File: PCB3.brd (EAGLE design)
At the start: 94.7 x 52.2 mm, 134 parts

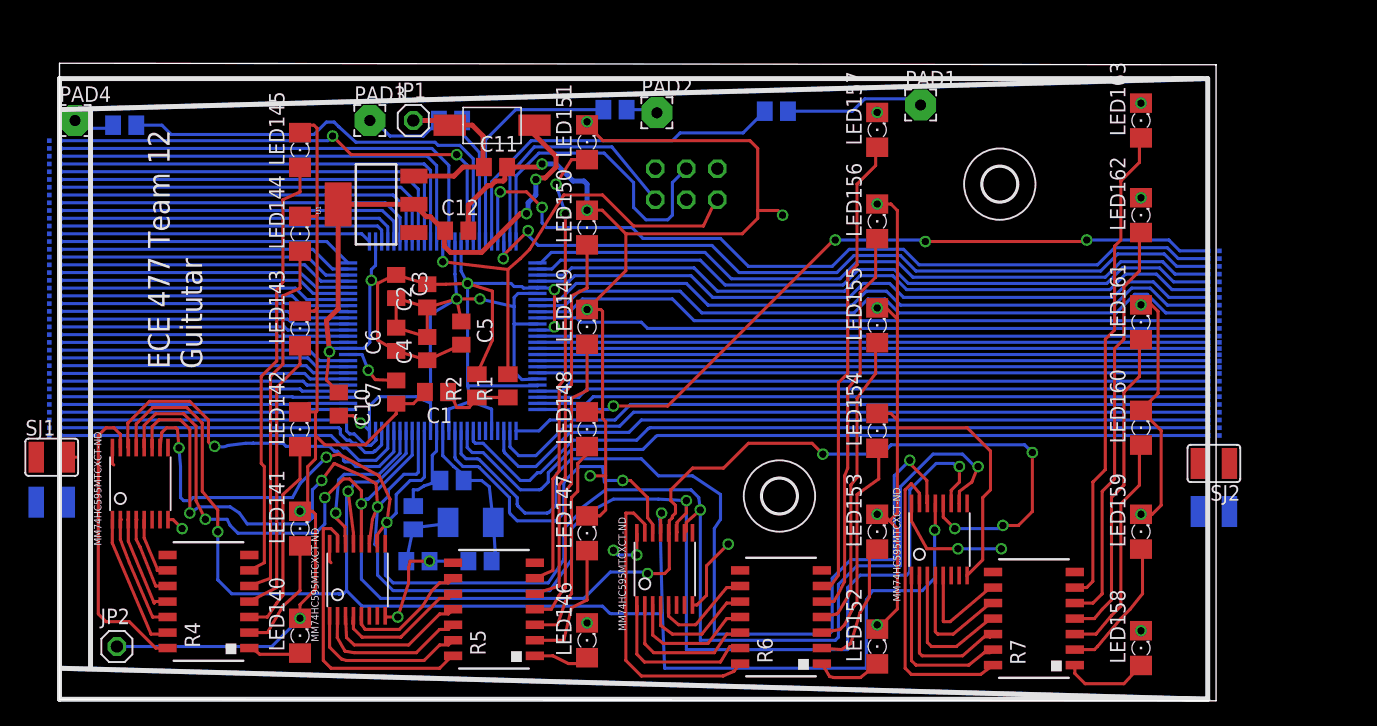
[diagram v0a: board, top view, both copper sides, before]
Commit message: Finished changing dimensions for PCB3 and switched out resistors for smaller ones.
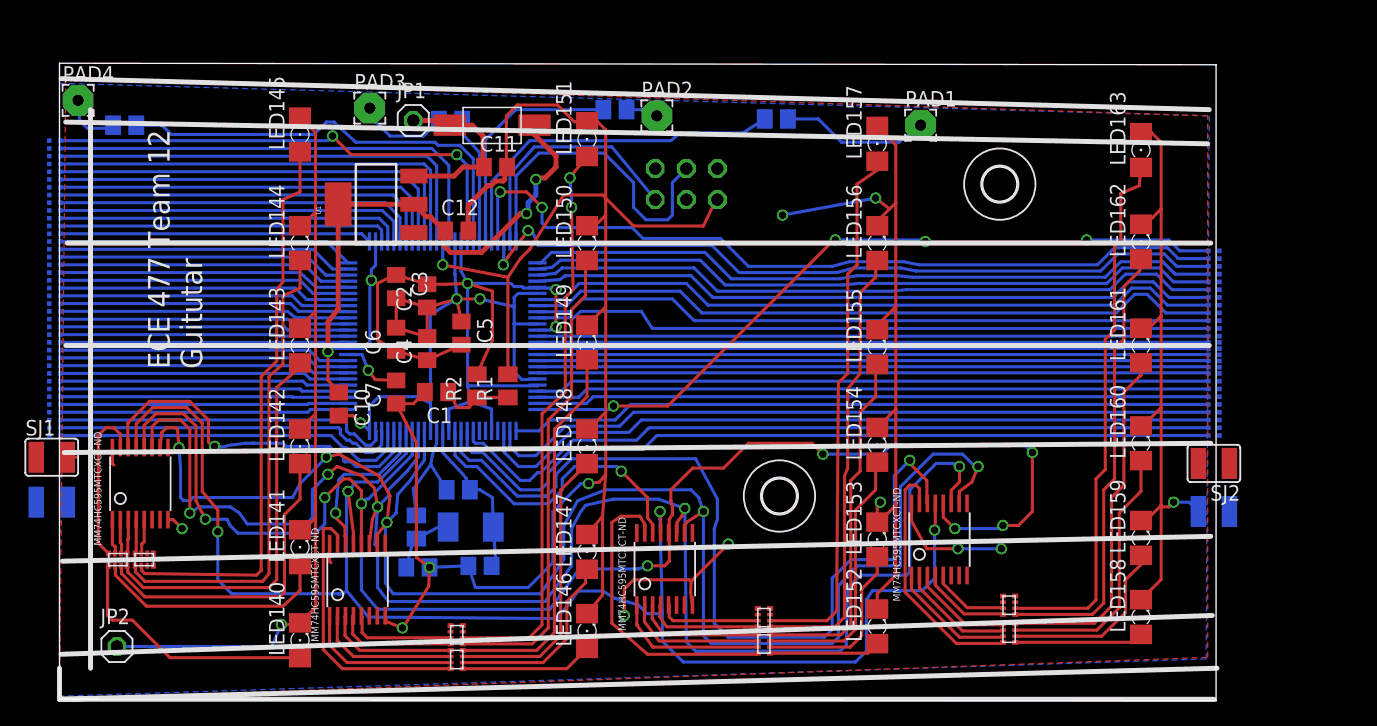
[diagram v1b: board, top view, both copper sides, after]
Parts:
- removed R4, R5, R6, R7: (no value), resistor-bourns:4814P
- added U$71, U$72, U$73, U$74, U$75, U$76, U$77, U$78: MNR04MRAPJ680, ECE477_Guitutar:MNR04
- moved LED158 2.54 mm to (88.5, 6.73)
- moved LED163 2.41 mm to (88.5, 45.0)
- moved LED162 2.16 mm to (88.5, 37.5)
- moved LED161 1.91 mm to (88.5, 29.0)
- moved LED155 1.78 mm to (66.9, 28.8)
- moved LED156 1.78 mm to (66.9, 37.3)
- moved PAD4 1.67 mm to (1.52, 49.0)
- moved LED152 1.65 mm to (66.9, 5.97)
- moved PAD1 1.65 mm to (70.5, 47.0)
- moved LED141 1.52 mm to (19.7, 12.4)
- moved LED147 1.52 mm to (43.2, 12.1)
- moved LED143 1.40 mm to (19.7, 29.0)
- moved LED142 1.40 mm to (19.7, 20.7)
- moved LED148 1.40 mm to (43.2, 20.7)
- moved LED145 1.27 mm to (19.7, 46.2)
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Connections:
- removed net N$102: LED153.A, R6.2
- removed net N$113: R7.13, U$26.1
- removed net N$114: R7.12, U$26.2
- removed net N$115: R7.11, U$26.3
- removed net N$116: R7.10, U$26.4
- removed net N$123: R7.9, U$26.5
- removed net N$127: LED160.A, R7.3
- removed net N$75: R5.9, U$28.5
- removed net N$78: LED146.A, R5.1
- removed net N$80: LED148.A, R5.3
- removed net N$81: LED149.A, R5.4
- removed net N$82: LED150.A, R5.5
- removed net N$83: LED151.A, R5.6
- removed net N$84: LED147.A, R5.2
- removed net N$90: R6.13, U$29.1
- removed net N$91: R6.12, U$29.2
- removed net N$92: R6.11, U$29.3
- removed net N$93: R6.10, U$29.4
- removed net N$94: R6.9, U$29.5
- removed net N$98: LED154.A, R6.3
- removed net N$99: LED155.A, R6.4
- new net N$10: LED148.A, U$75.P$3
- new net N$15: LED149.A, U$75.P$4
- new net N$17: LED150.A, U$76.P$1
- new net N$18: LED151.A, U$76.P$2
- new net N$19: U$27.1, U$73.P$6
- new net N$26: U$26.1, U$71.P$6
- new net N$27: U$26.2, U$71.P$7
- new net N$28: U$26.3, U$71.P$8
- new net N$29: U$26.4, U$72.P$5
- new net N$30: U$26.5, U$72.P$6
- new net N$36: U$29.1, U$77.P$6
- new net N$39: U$29.2, U$77.P$7
- new net N$40: U$29.3, U$77.P$8
- new net N$41: U$29.4, U$78.P$5
- new net N$42: U$29.5, U$78.P$6
- new net N$43: LED153.A, U$77.P$2
- new net N$44: LED154.A, U$77.P$3
- new net N$45: LED155.A, U$77.P$4
- new net N$6: U$28.5, U$76.P$6
- new net N$8: LED146.A, U$75.P$1
- new net N$9: LED147.A, U$75.P$2
- net N$100: now also U$78.P$1; no longer R6.5
- net N$101: now also U$78.P$2; no longer R6.6
- net N$125: now also U$71.P$5; no longer R7.14
- net N$126: now also U$71.P$1; no longer R7.1
- net N$134: now also U$71.P$4; no longer R7.4
- net N$135: now also U$72.P$1; no longer R7.5
- net N$136: now also U$72.P$2; no longer R7.6
- net N$137: now also U$71.P$2; no longer R7.2
- net N$20: now also U$27.2, U$73.P$7; no longer R4.13, U$27.1
- net N$21: now also U$27.3, U$73.P$8; no longer R4.12, U$27.2
- net N$22: now also U$27.4, U$74.P$5; no longer R4.11, U$27.3
- net N$23: now also U$27.5, U$74.P$6; no longer R4.10, U$27.4
- net N$24: now also LED142.A, U$73.P$3; no longer R4.9, U$27.5
- net N$31: now also U$73.P$5; no longer R4.14
- net N$32: now also U$73.P$1; no longer R4.1
- net N$33: now also U$73.P$2; no longer R4.2
- net N$34: now also LED160.A, U$71.P$3; no longer LED142.A, R4.3
- net N$35: now also U$73.P$4; no longer R4.4
- net N$46: now also U$74.P$1; no longer R4.5
- net N$47: now also U$74.P$2; no longer R4.6
- net N$62: now also U$75.P$6; no longer R5.13
- net N$63: now also U$75.P$7; no longer R5.12
- net N$64: now also U$75.P$8; no longer R5.11
- net N$74: now also U$76.P$5; no longer R5.10
- net N$77: now also U$75.P$5; no longer R5.14
- net N$96: now also U$77.P$5; no longer R6.14
- net N$97: now also U$77.P$1; no longer R6.1
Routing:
- net N$11: track 94.0 -> 0.00 mm
- net N$6: track 94.0 -> 8.82 mm
- net GND: track 261.6 -> 310.3 mm, vias 23 -> 11
- net N$18: track 0.00 -> 46.8 mm, vias 0 -> 2
- net N$17: track 0.00 -> 38.9 mm
- net N$83: track 37.4 -> 0.00 mm, vias 2 -> 0
- net N$15: track 0.00 -> 31.5 mm
- net N$82: track 31.1 -> 0.00 mm
- net N$45: track 0.00 -> 29.2 mm
- net N$99: track 24.5 -> 0.00 mm
- net N$81: track 24.4 -> 0.00 mm
- net N$10: track 0.00 -> 23.7 mm
- net LED_SER7: track 29.6 -> 51.8 mm
- net N$44: track 0.00 -> 21.8 mm
- net N$24: track 5.22 -> 26.0 mm
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
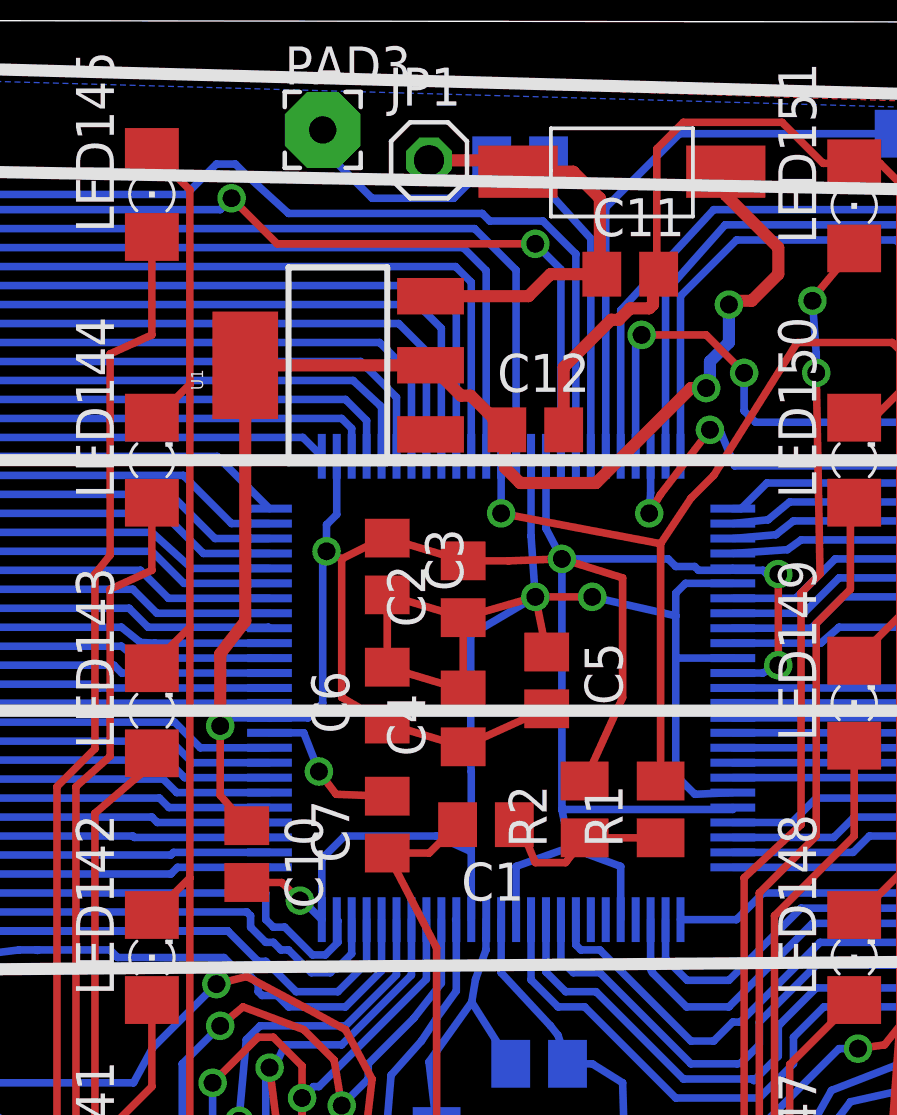
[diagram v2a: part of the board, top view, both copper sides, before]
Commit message: Updated ref des to match those in BOM
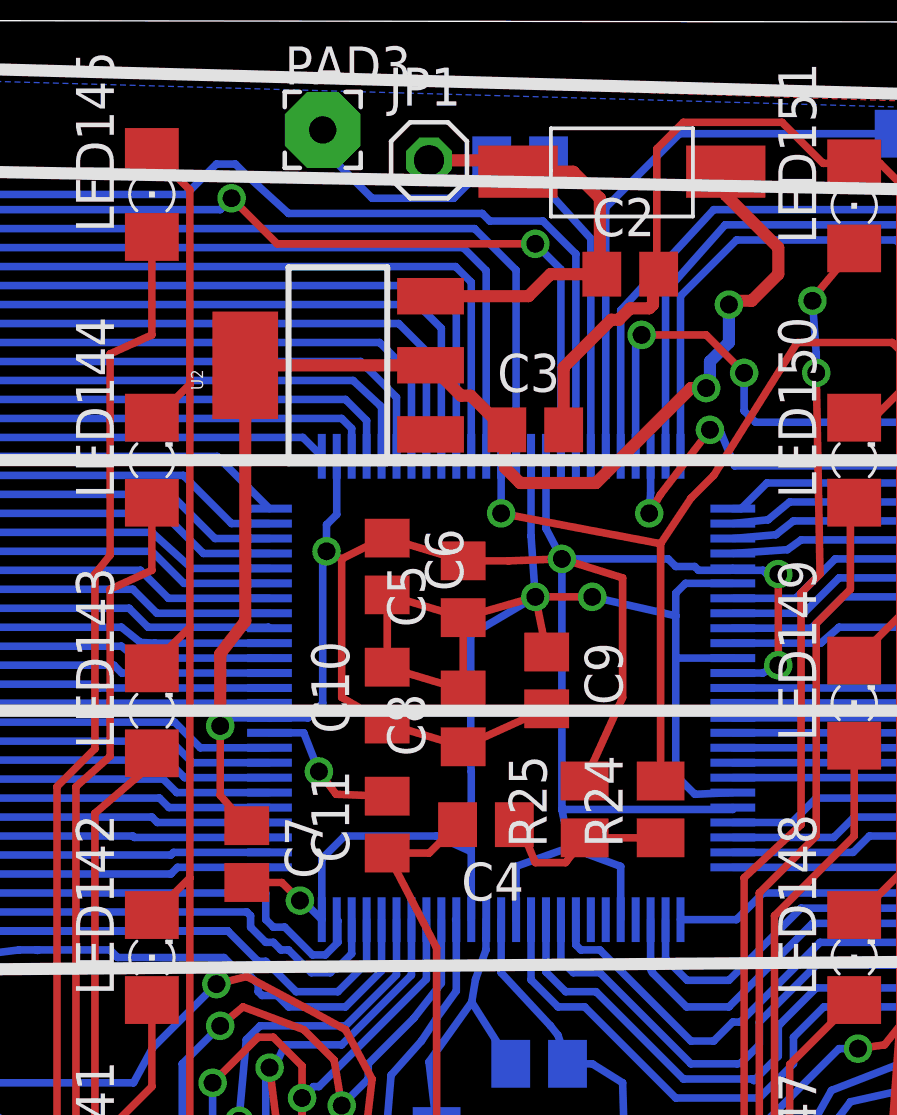
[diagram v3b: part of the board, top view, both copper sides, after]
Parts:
- removed C1: (no value), rcl:C0805
- removed R11: 330k, rcl:M0805
- removed U$2: PIC32MX570F512L, ECE477_Guitutar:TQFP100-14X14
- added C13: 9pF, rcl:C0805
- added R26: 1M, rcl:M0805
- added U2: (no value), SparkFun-IC-Power:SOT223
- C12: value 100uF -> 9pF
- C2: value (none) -> 10uF
- C3: value (none) -> 100uF
- C4: value (none) -> 0.1u
- R24: value (none) -> 1k
- R25: value (none) -> 10k
- R27: value (none) -> 100
- R8: value (none) -> 330k
- U1: value (none) -> PIC32MX570F512L; device SparkFun-IC-Power:SOT223 -> ECE477_Guitutar:TQFP100-14X14
- Y1: value (none) -> 16MHz
- moved R8 33.7 mm to (45.5, 48.3)
- moved C12 27.5 mm to (34.4, 10.9), flipped to the bottom, turned to 180 degrees
- moved R10 26.7 mm to (5.33, 47.0)
- moved R9 26.7 mm to (32.0, 47.4)
- moved C11 20.1 mm to (27.6, 25.1), turned to 90 degrees
- moved C9 19.5 mm to (32.9, 30.0), flipped to the top, turned to 270 degrees
- moved C8 18.3 mm to (30.1, 28.7), flipped to the top, turned to 90 degrees
- moved U1 12.1 mm to (31.4, 29.7), flipped to the bottom, turned to 180 degrees
- moved C2 11.9 mm to (35.7, 43.6), turned to 0 degrees
- moved C10 7.09 mm to (27.6, 29.5), turned to 90 degrees
- moved C3 6.74 mm to (32.5, 38.4), turned to 0 degrees
- moved C7 4.80 mm to (22.9, 24.2), turned to 270 degrees
- moved C6 4.32 mm to (27.6, 33.8), turned to 270 degrees
- moved C5 4.13 mm to (30.1, 33.0), turned to 90 degrees
- moved C4 3.64 mm to (30.9, 25.1), turned to 180 degrees
- renumbered D1 to D140, R1 to R24, R12 to R7, R2 to R25, R3 to R27
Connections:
- removed net N$124: U$26.16
- removed net N$25: U$27.16
- removed net N$76: U$28.16
- removed net N$95: U$29.16
- net 5.2V_PB: now also C2.1, U2.3; no longer C11.1, U1.3
- net AMP: now also U1.50; no longer U$2.50
- net EAN: now also U1.79; no longer U$2.79
- net FRET1: now also U1.93; no longer U$2.93
- net FRET10: now also U1.22; no longer U$2.22
- net FRET11: now also U1.23; no longer U$2.23
- net FRET12: now also U1.26; no longer U$2.26
- net FRET13: now also U1.27; no longer U$2.27
- net FRET14: now also U1.28; no longer U$2.28
- net FRET15: now also U1.29; no longer U$2.29
- net FRET16: now also U1.32; no longer U$2.32
- net FRET17: now also U1.33; no longer U$2.33
- net FRET18: now also U1.34; no longer U$2.34
- net FRET19: now also U1.35; no longer U$2.35
- net FRET2: now also U1.92; no longer U$2.92
- net FRET20: now also U1.38; no longer U$2.38
- net FRET21: now also U1.39; no longer U$2.39
- net FRET22: now also U1.40; no longer U$2.40
- net FRET3: now also U1.91; no longer U$2.91
- net FRET4: now also U1.90; no longer U$2.90
- net FRET5: now also U1.17; no longer U$2.17
- net FRET6: now also R10.1, U1.18; no longer R9.1, U$2.18
- net FRET7: now also R9.1, U1.19; no longer R10.1, U$2.19
- net FRET8: now also R8.1, U1.20; no longer R11.1, U$2.20
- net FRET9: now also U1.21; no longer U$2.21
- net G: now also U1.69; no longer U$2.69
- net GND: now also C11.1, C12.1, C13.1, C2.2, C3.2, C4.2; no longer C1.2, C11.2, C12.2, C7.1, C8.1, C9.1
- net LED_SER1: now also U1.100; no longer U$2.100
- net LED_SER10: now also U1.70; no longer U$2.70
- net LED_SER11: now also U1.61; no longer U$2.61
- net LED_SER12: now also U1.51; no longer U$2.51
- net LED_SER13: now also U1.58; no longer U$2.58
- net LED_SER14: now also U1.59; no longer U$2.59
- net LED_SER15: now also U1.53; no longer U$2.53
- net LED_SER16: now also U1.52; no longer U$2.52
- net LED_SER17: now also U1.41; no longer U$2.41
- net LED_SER18: now also U1.42; no longer U$2.42
- net LED_SER19: now also U1.43; no longer U$2.43
- net LED_SER2: now also U1.99; no longer U$2.99
- net LED_SER20: now also U1.44; no longer U$2.44
- net LED_SER21: now also U1.47; no longer U$2.47
- net LED_SER22: now also U1.48; no longer U$2.48
- net LED_SER23: now also U1.49; no longer U$2.49
- net LED_SER3: now also U1.98; no longer U$2.98
- net LED_SER4: now also U1.97; no longer U$2.97
- net LED_SER5: now also U1.74; no longer U$2.74
- net LED_SER6: now also U1.73; no longer U$2.73
- net LED_SER7: now also U1.72; no longer U$2.72
- net LED_SER8: now also U1.60; no longer U$2.60
- net LED_SER9: now also U1.71; no longer U$2.71
- net N$1: now also C4.1; no longer C1.1
- net N$12: now also C11.2, U1.85; no longer C7.2, U$2.85
- net N$13: now also U1.13; no longer U$2.13
- net N$14: now also U1.25; no longer U$2.25
- net N$2: now also U1.24; no longer U$2.24
- net N$37: now also C13.2; no longer C9.2
- net N$38: now also C12.2, R26.2, U1.63; no longer C8.2, R8.2, U$2.63
- net N$4: now also R8.2; no longer R11.2
- net N$5: now also R9.2; no longer R10.2
- net N$7: now also R10.2; no longer R9.2
- net OSC2: now also R26.1, U1.64; no longer R8.1, U$2.64
- net P0_0: now also U1.82; no longer U$2.82
- net P0_4: now also U1.3; no longer U$2.3
- net P0_5: now also U1.83; no longer U$2.83
- net P1_2: now also U1.76; no longer U$2.76
- net P1_3: now also U1.77; no longer U$2.77
- net P1_5: now also U1.1; no longer U$2.1
- net P1_7: now also U1.84; no longer U$2.84
- net P2_0: now also U1.81; no longer U$2.81
- net P2_4: now also U1.80; no longer U$2.80
- net P3_1: now also U1.11; no longer U$2.11
- net P3_2: now also U1.10; no longer U$2.10
- net P3_3: now also U1.9; no longer U$2.9
- net P3_4: now also U1.8; no longer U$2.8
- net P3_6: now also U1.7; no longer U$2.7
- net P3_7: now also U1.6; no longer U$2.6
- net RCK: now also U1.68; no longer U$2.68
- net RST_N: now also U1.78; no longer U$2.78
- net RXD: now also U1.14; no longer U$2.14
- net SCK: now also U1.67; no longer U$2.67
- net SCLR: now also U1.66; no longer U$2.66
- net STRING1: now also U1.96; no longer U$2.96
- net STRING2: now also U1.95; no longer U$2.95
- net STRING3: now also U1.94; no longer U$2.94
- net STRING4: now also U1.89; no longer U$2.89
- net STRING5: now also U1.88; no longer U$2.88
- net STRING6: now also U1.87; no longer U$2.87
- net SW_BTN: now also U1.4; no longer U$2.4
- net TXD: now also U1.12; no longer U$2.12
- net VDD: now also C7.1, C8.1, C9.2, U$26.16, U$27.16, U$28.16, U$29.16, U1.16, U1.30, U1.37, U1.46, U1.55, U1.62, U1.86, U2.2, U2.4; no longer C12.1, C2.2, C4.1, U$2.16, U$2.2, U$2.30, U$2.37, U$2.46, U$2.55, U$2.62, U$2.86, U1.4
- net VSS: now also C7.2, C8.2, C9.1, U1.15, U1.31, U1.36, U1.45, U1.65, U1.75; no longer C2.1, C3.2, C4.2, U$2.15, U$2.31, U$2.36, U$2.45, U$2.65, U$2.75
- net WAKEUP: now also U1.5; no longer U$2.5
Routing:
- net VDD: track 125.6 -> 138.8 mm, vias 7 -> 9
- net N$124: track 10.1 -> 0.00 mm, vias 2 -> 0
- net N$76: track 1.60 -> 0.00 mm
- net N$25: track 1.47 -> 0.00 mm
